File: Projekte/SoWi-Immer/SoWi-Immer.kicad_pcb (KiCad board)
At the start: 2 copper layers, 42 x 12.3 mm, 14 parts, among them P1 CONN_01X02, U1 SPV1040

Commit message: Diverse Dateien hinzugefügt
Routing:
- net Net-(D2-Pad2): track 0.00 -> 6.10 mm
- net Net-(D3-Pad2): track 0.00 -> 2.86 mm
- net Net-(D1-Pad2): track 0.00 -> 2.85 mm
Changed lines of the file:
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@@
   (general
     (links 23)
-    (no_connects 23)
-    (area 139.949999 79.949999 182.050001 92.350001)
+    (no_connects 20)
+    (area 139.949999 78.158599 182.050001 94.558033)
     (thickness 1.6)
     (drawings 4)
-    (tracks 0)
+    (tracks 4)
     (zones 0)
     (modules 14)
@@
   (gr_line (start 182 80) (end 182 92.3) (angle 90) (layer Edge.Cuts) (width 0.1))
   (gr_line (start 140 80) (end 140 92.3) (angle 90) (layer Edge.Cuts) (width 0.1))
+  (segment (start 159.4 83.15) (end 162.25 83.15) (width 0.25) (layer F.Cu) (net 4) (status C00000))
+  (segment (start 141.4 83.15) (end 141.4 89.25) (width 0.25) (layer F.Cu) (net 5) (status C00000))
+  (segment (start 162.2581 89.258) (end 159.408 89.258) (width 0.25) (layer F.Cu) (net 6) (status C00000))
+  (segment (start 159.408 89.258) (end 159.4 89.25) (width 0.25) (layer F.Cu) (net 6) (status C00000))
 )

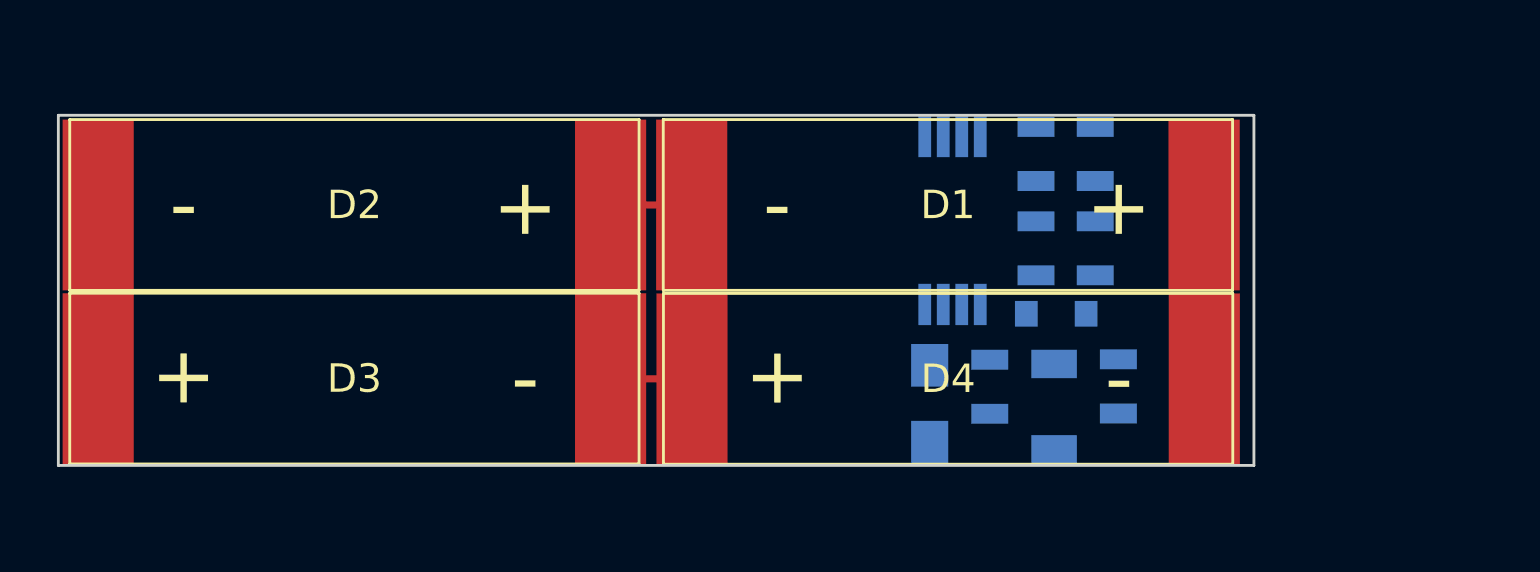
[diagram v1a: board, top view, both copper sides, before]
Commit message: Schematic & PCB geändert
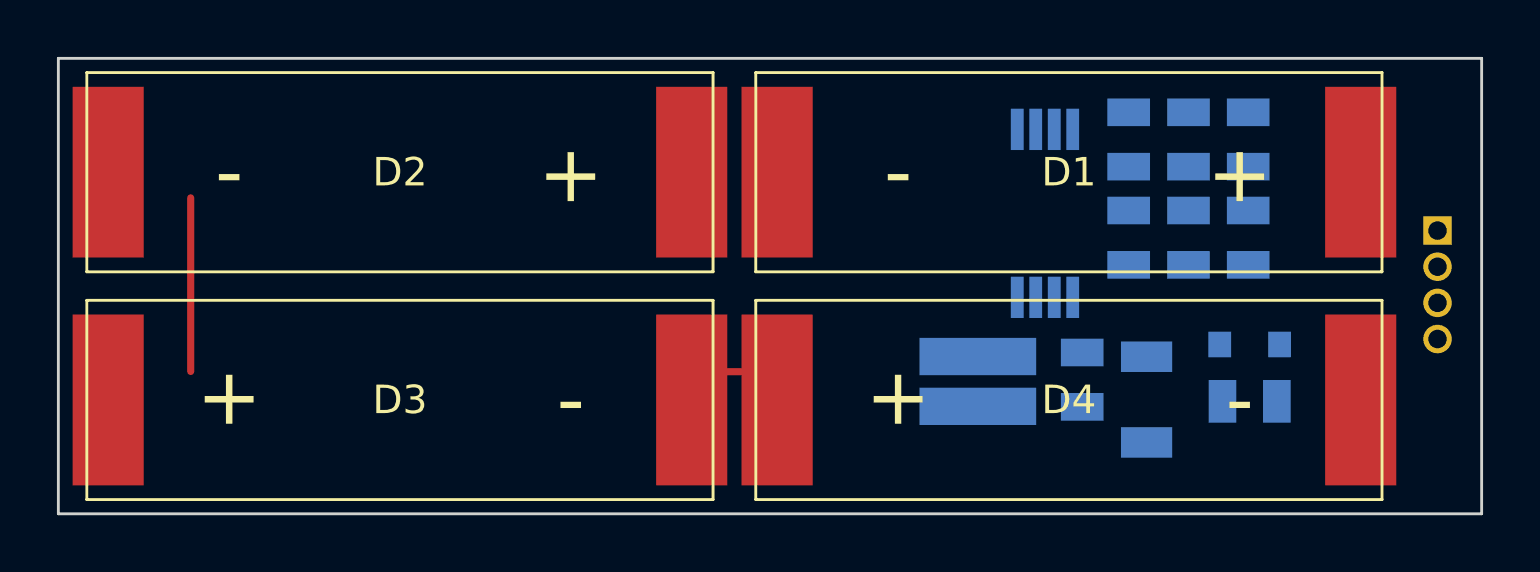
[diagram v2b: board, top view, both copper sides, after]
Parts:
- added R6: 0, Resistor_SMD:R_0805_2012Metric, B.Cu at (181.8, 80.8)
- added R7: 0, Resistor_SMD:R_0805_2012Metric, B.Cu at (181.8, 84.3)
- added R8: 0, Resistor_SMD:R_0805_2012Metric, B.Cu at (181.8, 90.0)
- C1: footprint Capacitors_SMD:C_1206 -> Capacitor_SMD:C_1206_3216Metric
- L1: footprint Resistors_SMD:R_0805_HandSoldering -> Resistor_SMD:R_0815_2038Metric
- P1: value CONN_01X02 -> CONN_01X04; footprint Resistors_SMD:R_0805 -> Connector_PinHeader_1.27mm:PinHeader_1x04_P1.27mm_Vertical
- R1, R2, R3, R4, R5: footprint Resistors_SMD:R_0805 -> Resistor_SMD:R_0805_2012Metric
- U1: footprint SSOP_Packages:TSSOP-8_4.4x3mm_Pitch0.65mm -> Package_SSOP:TSSOP-8_4.4x3mm_P0.65mm
- moved P1 12.5 mm to (188.4, 84.0), turned to 180 degrees
- moved D5 6.88 mm to (181.8, 88.0)
- moved D1 4.40 mm to (175.5, 82.0)
- moved D4 4.31 mm to (175.5, 90.0)
- moved R5 3.31 mm to (179.7, 80.8)
- moved R2 3.30 mm to (177.6, 80.8)
- moved R4 3.29 mm to (179.7, 84.3)
- moved R1 3.28 mm to (177.6, 84.3)
- moved C1 3.26 mm to (178.2, 90.0)
- moved R3 3.26 mm to (176.0, 89.3)
- moved U1 3.26 mm to (174.7, 83.4)
- moved D2 1.97 mm to (152.0, 82.0)
- moved L1 1.86 mm to (172.3, 89.3)
- moved D3 1.77 mm to (152.0, 90.0)
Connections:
- D4 pad 2: GND -> Net-(D4-Pad2)
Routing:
- net Net-(D2-Pad2): track 6.10 -> 0.00 mm
- net (no net): track 0.00 -> 6.10 mm
- net Net-(D1-Pad2): track 2.85 -> 0.00 mm
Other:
- board size 42 x 12.3 mm -> 50 x 16 mm

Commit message: Kléine Laxoutanpassung
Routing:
- net Net-(D2-Pad2): track 0.00 -> 8.07 mm
- net (no net): track 6.10 -> 0.00 mm
- added copper zone on F.Cu, net Net-(D2-Pad2)
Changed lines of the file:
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@@
   (general
     (links 30)
-    (no_connects 29)
+    (no_connects 28)
     (area 139.949999 77.949999 190.050001 94.050001)
     (thickness 1.6)
     (drawings 4)
-    (tracks 3)
+    (tracks 5)
     (zones 0)
     (modules 17)
@@
     (last_trace_width 0.25)
     (trace_clearance 0.2)
-    (zone_clearance 0.508)
+    (zone_clearance 0.2)
     (zone_45_only no)
     (trace_min 0.2)
@@
   (gr_line (start 190 78) (end 140 78) (angle 90) (layer Edge.Cuts) (width 0.1))
   (gr_line (start 140 78) (end 140 94) (angle 90) (layer Edge.Cuts) (width 0.1))
-  (segment (start 144.65 82.9) (end 144.65 89) (width 0.25) (layer F.Cu) (net 0))
+  (segment (start 141.75 90) (end 141.75 85.85) (width 0.25) (layer F.Cu) (net 5) (status 400000))
+  (segment (start 141.75 82) (end 141.75 85.85) (width 0.25) (layer F.Cu) (net 5) (status 400000))
+  (segment (start 141.75 85.85) (end 141.7 85.9) (width 0.25) (layer F.Cu) (net 5))
   (segment (start 165.5081 89.008) (end 162.658 89.008) (width 0.25) (layer F.Cu) (net 6))
   (segment (start 162.658 89.008) (end 162.65 89) (width 0.25) (layer F.Cu) (net 6))
+  (zone (net 5) (net_name "Net-(D2-Pad2)") (layer F.Cu) (hatch edge 0.508)
+    (connect_pads yes (clearance 0.2))
+    (min_thickness 0.1)
+    (fill yes (arc_segments 16) (thermal_gap 0.508) (thermal_bridge_width 0.508))
+    (polygon
+      (pts
+        (xy 143 87.25) (xy 140.5 87.25) (xy 140.5 84.65) (xy 143 84.65)
+      )
+    )
+  )
 )
